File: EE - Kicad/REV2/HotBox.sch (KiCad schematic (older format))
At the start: 30 parts, among them J1 Conn_01x02, J2 Conn_01x01, J3 Conn_01x01, M1 Fan_4pin, M2 Fan, Q1 BSC028N06LS3, Q2 PUMH11, Q4 PUMD3,115, SW1 SW_Push_4PIN, SW2 SW_Push_4PIN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

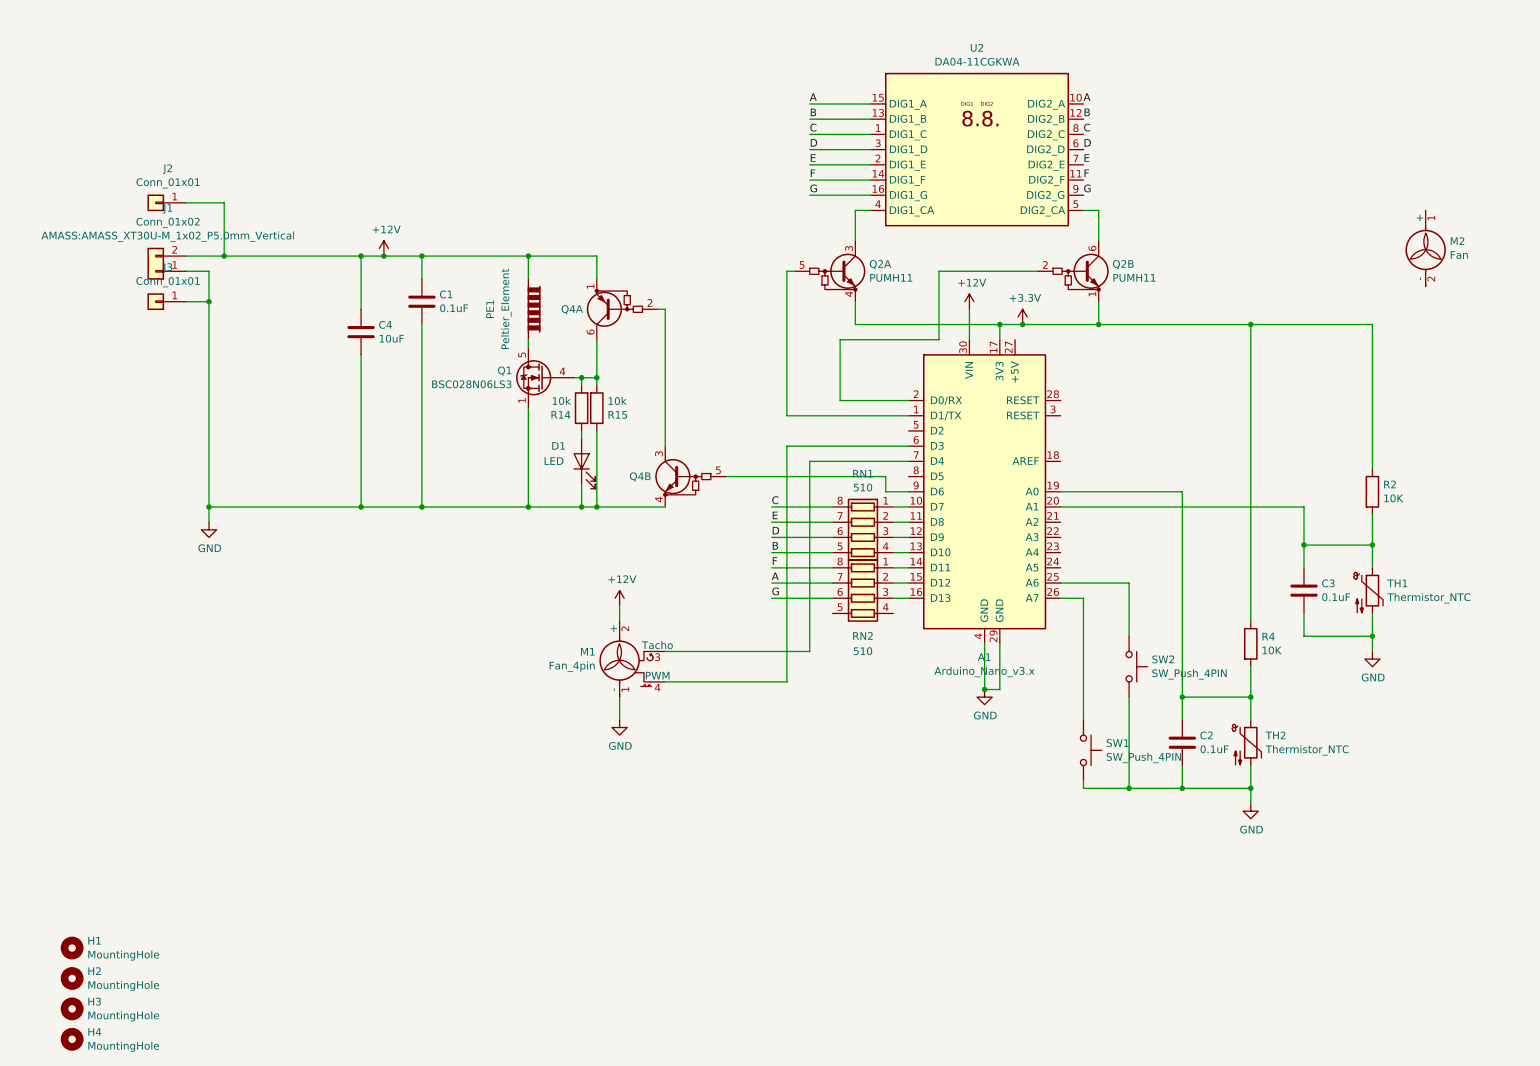
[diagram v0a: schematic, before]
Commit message: Committing 2nd REV.  Update PCB to fix issues with REV1.  Reduce mechanical size.
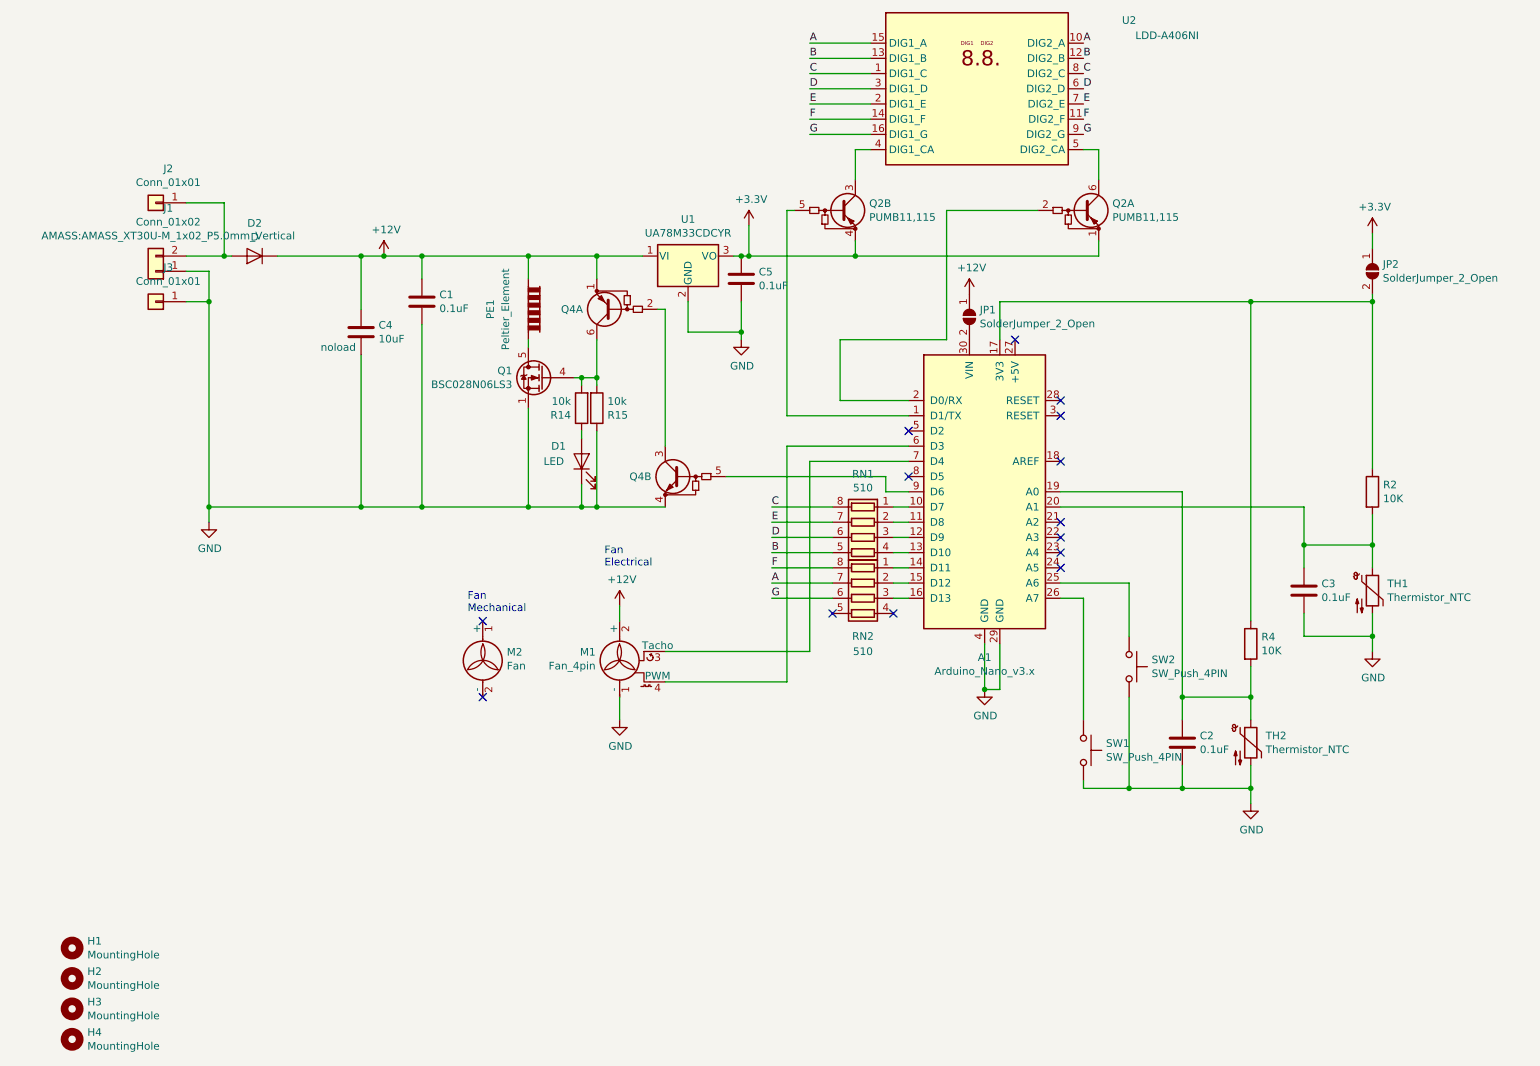
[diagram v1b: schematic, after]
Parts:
- removed Q2: PUMH11, Package_TO_SOT_SMD:SOT-363_SC-70-6_Handsoldering, symbol Device:Q_DUAL_NPN_NPN_BRT_E1B1C2E2B2C1
- added C5: 0.1uF, AEvan:0805_C, symbol Device:C
- added D2: D, Diode_SMD:D_SMA, symbol Device:D
- added JP1, JP2: SolderJumper_2_Open, Jumper:SolderJumper-2_P1.3mm_Open_TrianglePad1.0x1.5mm, symbol Jumper:SolderJumper_2_Open
- added Q2: PUMB11,115, Package_TO_SOT_SMD:SOT-363_SC-70-6_Handsoldering, symbol Device:Q_DUAL_PNP_PNP_BRT_E1B1C2E2B2C1
- added U1: UA78M33CDCYR, Package_TO_SOT_SMD:SOT-223-3_TabPin2, symbol Regulator_Linear:LT1129-3.3_SOT223
- A1: DigikeyPN (none) -> 497-19489-ND; manf# (none) -> NUCLEO-G431KB
- C1, C2, C3: DigikeyPN (none) -> 478-12790-1-ND; manf# (none) -> 08055D104KAT2A
- C4: DigikeyPN (none) -> 493-16595-ND; fit_field (none) -> noload; manf# (none) -> RS81C101MDN1
- D1: DigikeyPN (none) -> 732-4978-1-ND; manf# (none) -> 150060RS75000
- H1, H2, H3, H4: DigikeyPN (none) -> 335-1156-ND; manf# (none) -> RM3X6MM 2701
- J1: DigikeyPN (none) -> Amass XT30
- J2, J3: DigikeyPN (none) -> 36-575-4-ND; manf# (none) -> 575-4
- M1: DigikeyPN (none) -> S1012EC-04-ND; manf# (none) -> PREC004SAAN-RC
- M2: DigikeyPN (none) -> Intel E98290-001
- PE1: DigikeyPN (none) -> TEC1-12706
- Q1: DigikeyPN (none) -> 1727-5435-1-ND; manf# (none) -> PSMN9R1-30YL\\,115
- Q4: manf# (none) -> PUMD3\\,165
- R14, R15, R2, R4: manf# (none) -> CRCW080510K0JNEAC
- RN1, RN2: manf# (none) -> YC164-JR-07510RL
- SW1, SW2: manf# (none) -> D6R60 F2 LFS
- TH1, TH2: DigikeyPN (none) -> 445-175460-1-ND; manf# (none) -> NTCG203NH103JT1
- U2: value DA04-11CGKWA -> LDD-A406NI; DigikeyPN (none) -> 67-1447-ND; manf# (none) -> LDD-A406NI
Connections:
- net +12V: now also D2.1 (K), JP1.1 (A), U1.1 (VI); no longer A1.30 (VIN), J1.2 (Pin_2), J2.1 (Pin_1)
- net +3V3: now also C5.1, JP2.1 (A), Q2.1 (E1), Q2.4 (E2), U1.3 (VO); no longer A1.17 (3V3), R2.1, R4.1
- net GND: now also C5.2, U1.2 (GND)
- net at A1.1 (D1/TX): now also Q2.5 (B2)
- net at A1.2 (D0/RX): now also Q2.2 (B1)
- net at U2.4 (DIG1_CA): now also Q2.3 (C2)
- net at U2.5 (DIG2_CA): now also Q2.6 (C1)
- new net: D2.2 (A), J1.2 (Pin_2), J2.1 (Pin_1)
- new net: A1.17 (3V3), JP2.2 (B), R2.1, R4.1
- new net: A1.30 (VIN), JP1.2 (B)
- no-connect marks 0 -> 14
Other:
- note added: "Fan\nElectrical\n"
- note added: "Fan\nMechanical"
- moved on the sheet: M2, U2
